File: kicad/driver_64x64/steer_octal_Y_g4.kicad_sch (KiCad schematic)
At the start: 66 parts

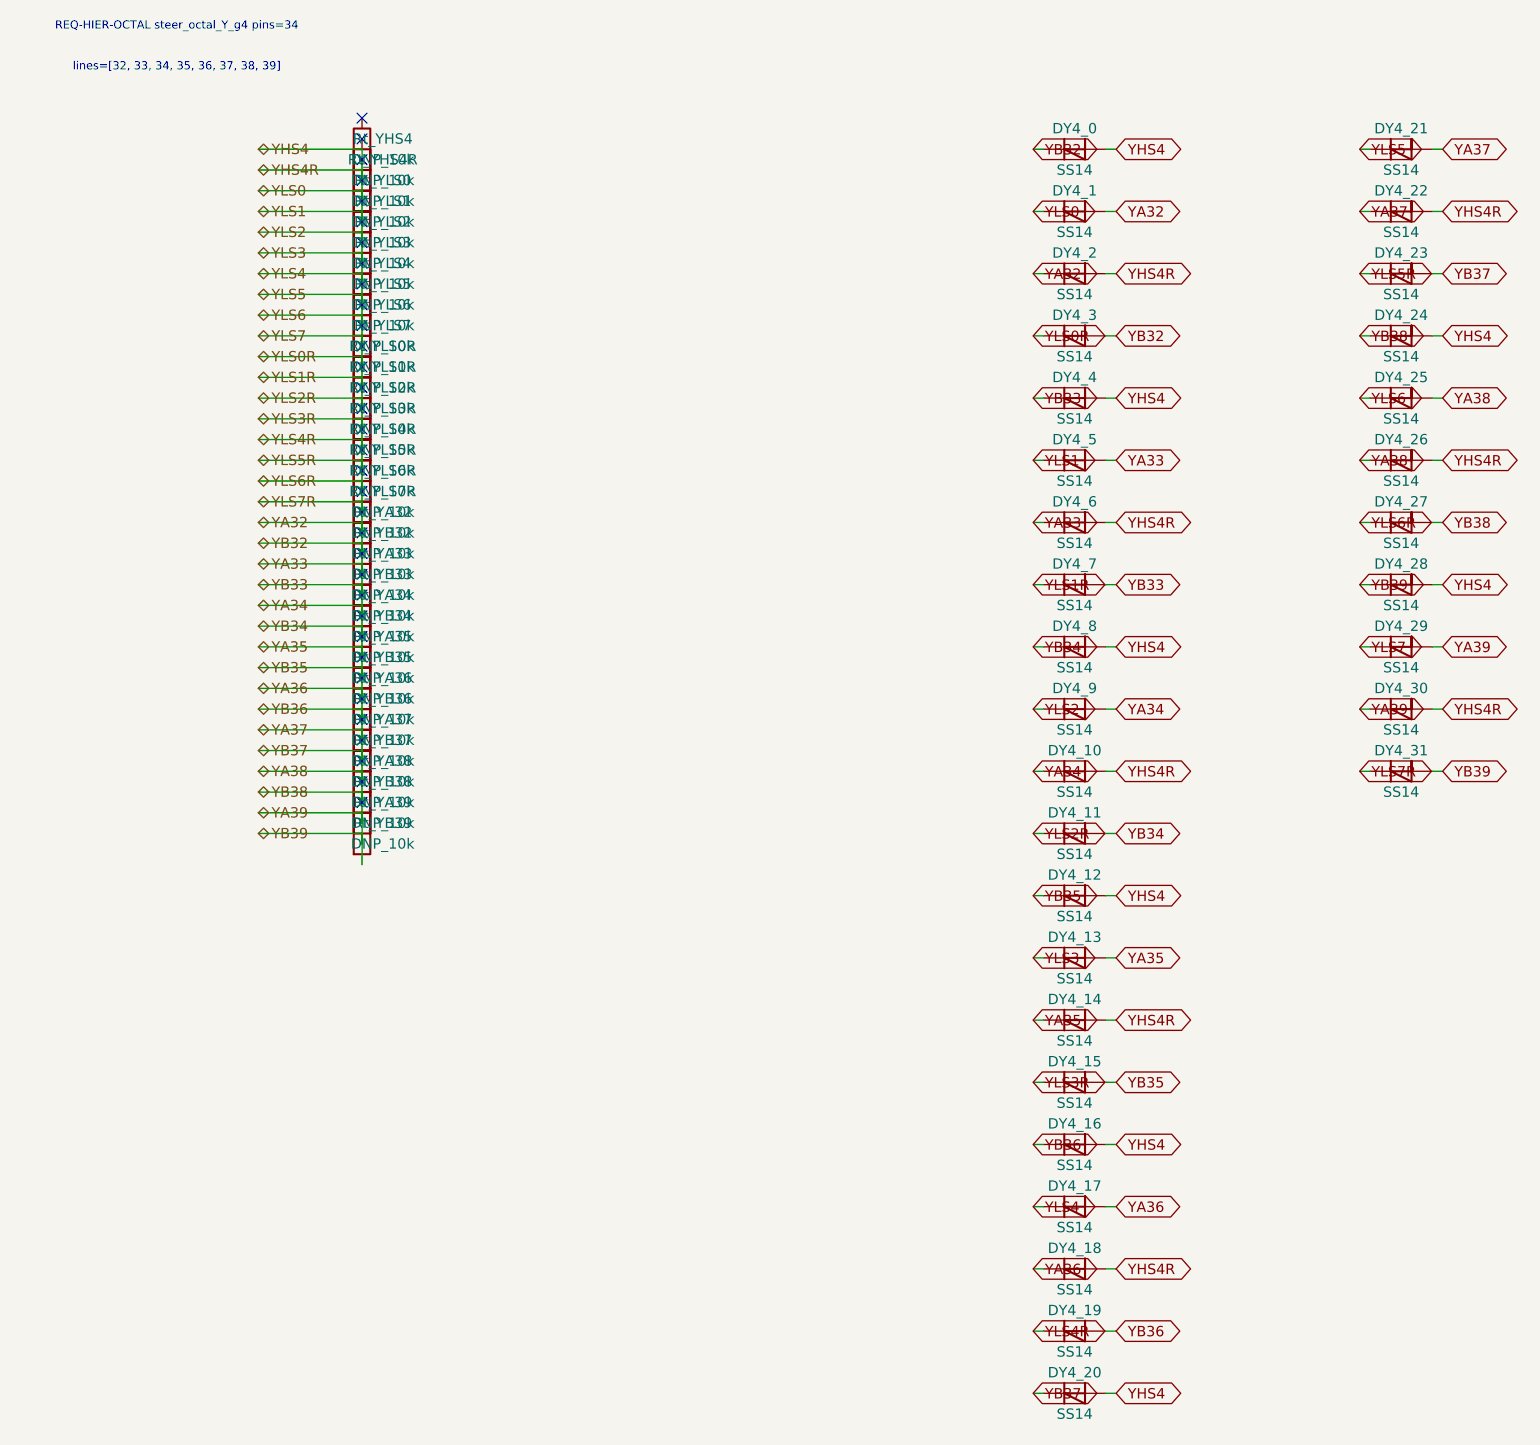
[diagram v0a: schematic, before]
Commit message: logical seperation into host and multiple decode/drive/steering boards
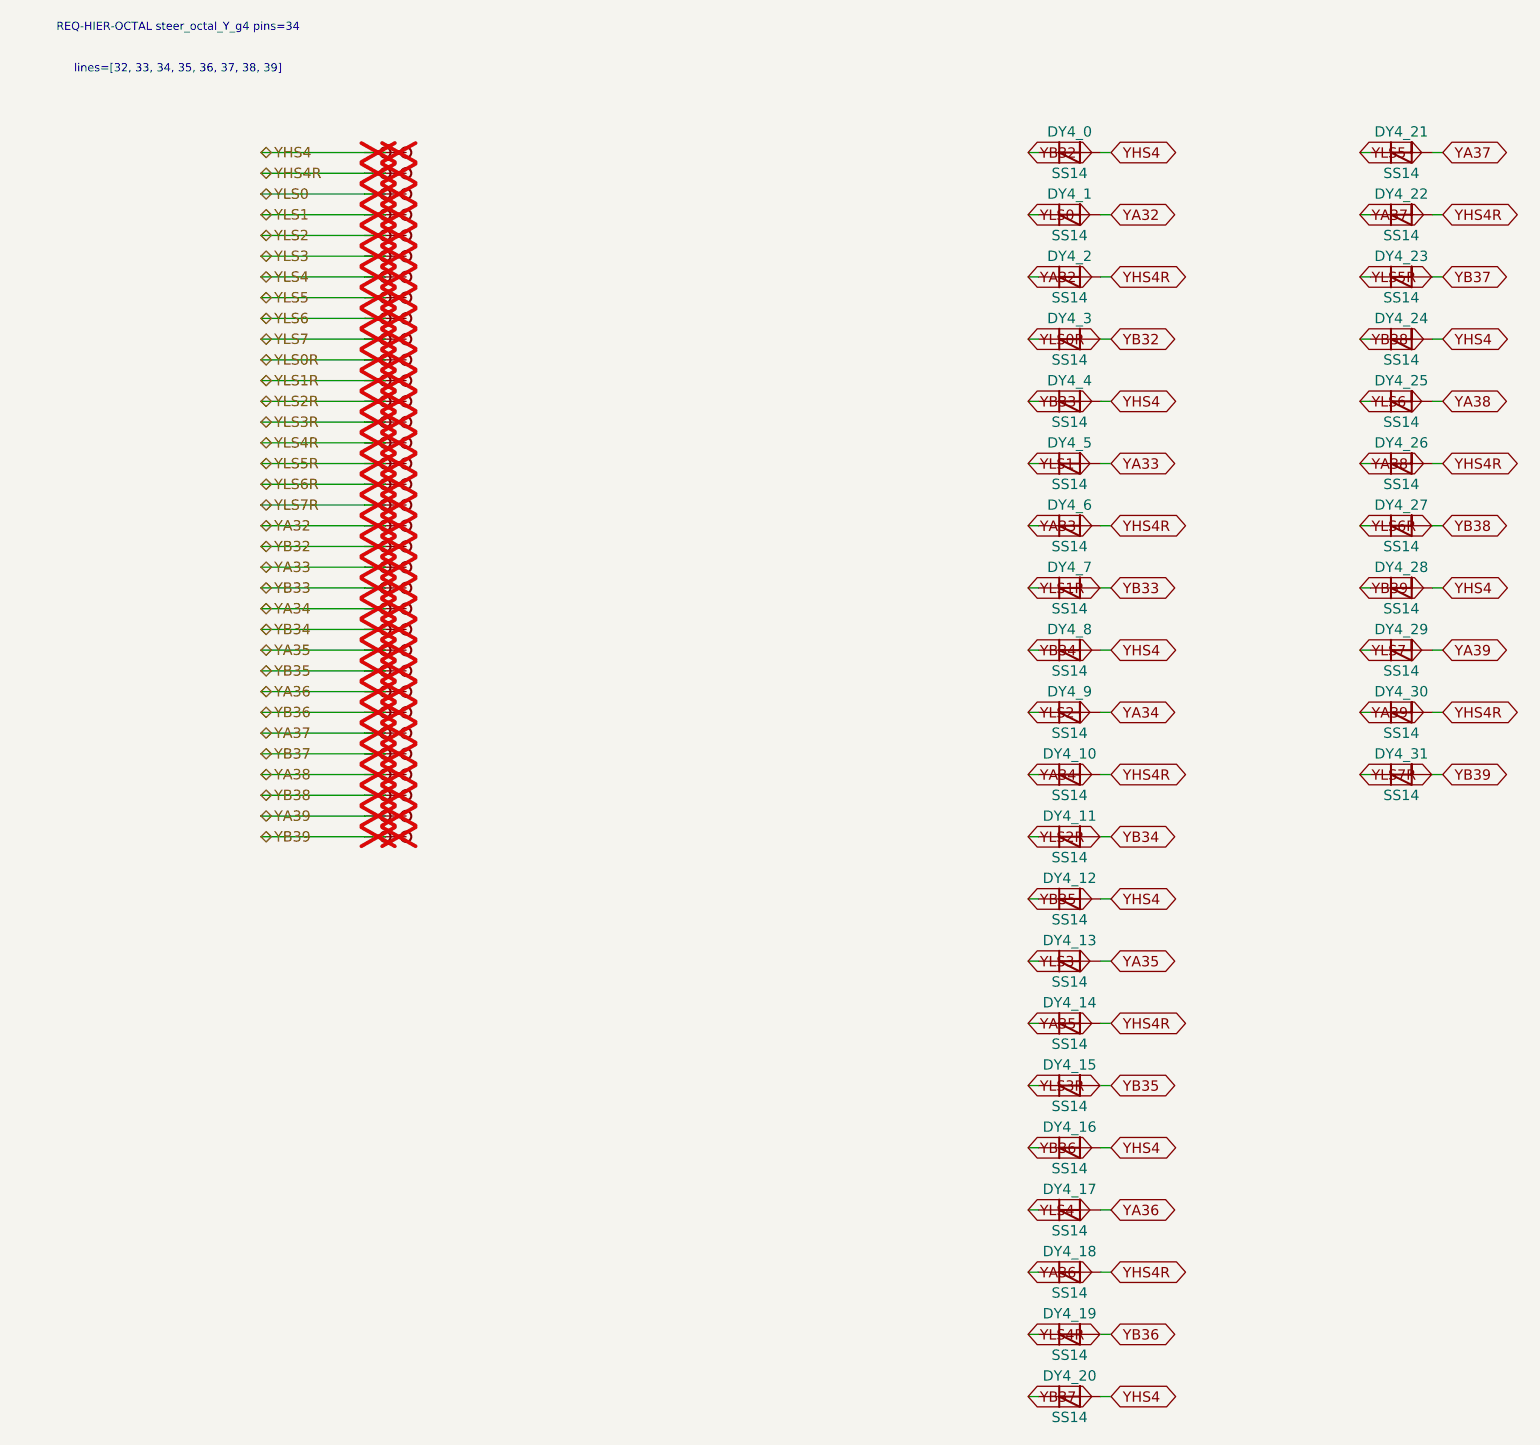
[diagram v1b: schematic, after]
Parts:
- removed Rt_YA32, Rt_YA33, Rt_YA34, Rt_YA35, Rt_YA36, Rt_YA37, Rt_YA38, Rt_YA39, Rt_YB32, Rt_YB33, Rt_YB34, Rt_YB35, Rt_YB36, Rt_YB37, Rt_YB38, Rt_YB39, Rt_YHS4, Rt_YHS4R, Rt_YLS0, Rt_YLS0R, Rt_YLS1, Rt_YLS1R, Rt_YLS2, Rt_YLS2R, Rt_YLS3, Rt_YLS3R, Rt_YLS4, Rt_YLS4R, Rt_YLS5, Rt_YLS5R, Rt_YLS6, Rt_YLS6R, Rt_YLS7, Rt_YLS7R: DNP_10k, symbol Device:R
- added TP_YA32, TP_YA32b, TP_YA33, TP_YA33b, TP_YA34, TP_YA34b, TP_YA35, TP_YA35b, TP_YA36, TP_YA36b, TP_YA37, TP_YA37b, TP_YA38, TP_YA38b, TP_YA39, TP_YA39b, TP_YB32, TP_YB32b, TP_YB33, TP_YB33b, TP_YB34, TP_YB34b, TP_YB35, TP_YB35b, TP_YB36, TP_YB36b, TP_YB37, TP_YB37b, TP_YB38, TP_YB38b, TP_YB39, TP_YB39b, TP_YHS4, TP_YHS4R, TP_YHS4Rb, TP_YHS4b, TP_YLS0, TP_YLS0R, TP_YLS0Rb, TP_YLS0b, TP_YLS1, TP_YLS1R, TP_YLS1Rb, TP_YLS1b, TP_YLS2, TP_YLS2R, TP_YLS2Rb, TP_YLS2b, TP_YLS3, TP_YLS3R, TP_YLS3Rb, TP_YLS3b, TP_YLS4, TP_YLS4R, TP_YLS4Rb, TP_YLS4b, TP_YLS5, TP_YLS5R, TP_YLS5Rb, TP_YLS5b, TP_YLS6, TP_YLS6R, TP_YLS6Rb, TP_YLS6b, TP_YLS7, TP_YLS7R, TP_YLS7Rb, TP_YLS7b: Stub, symbol CMR:Stub
- DY4_0, DY4_1, DY4_10, DY4_11, DY4_12, DY4_13, DY4_14, DY4_15, DY4_16, DY4_17, DY4_18, DY4_19, DY4_2, DY4_20, DY4_21, DY4_22, DY4_23, DY4_24, DY4_25, DY4_26, DY4_27, DY4_28, DY4_29, DY4_3, DY4_30, DY4_31, DY4_4, DY4_5, DY4_6, DY4_7, DY4_8, DY4_9: symbol Device:D_Schottky -> CMR:D_Schottky
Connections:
- net YA32: now also TP_YA32.1, TP_YA32b.1; no longer DY4_0.1 (K), DY4_0.2 (A), DY4_1.1 (K), DY4_10.1 (K), DY4_10.2 (A), DY4_11.1 (K), DY4_11.2 (A), DY4_12.1 (K), DY4_12.2 (A), DY4_13.1 (K), DY4_13.2 (A), DY4_14.1 (K), DY4_14.2 (A), DY4_15.1 (K), DY4_15.2 (A), DY4_16.1 (K), DY4_16.2 (A), DY4_17.1 (K), DY4_17.2 (A), DY4_18.1 (K), DY4_18.2 (A), DY4_19.1 (K), DY4_19.2 (A), DY4_2.2 (A), DY4_20.1 (K), DY4_20.2 (A), DY4_21.1 (K), DY4_21.2 (A), DY4_22.1 (K), DY4_22.2 (A), DY4_23.1 (K), DY4_23.2 (A), DY4_24.1 (K), DY4_24.2 (A), DY4_25.1 (K), DY4_25.2 (A), DY4_26.1 (K), DY4_26.2 (A), DY4_27.1 (K), DY4_27.2 (A), DY4_28.1 (K), DY4_28.2 (A), DY4_29.1 (K), DY4_29.2 (A), DY4_3.1 (K), DY4_3.2 (A), DY4_30.1 (K), DY4_30.2 (A), DY4_31.1 (K), DY4_31.2 (A), DY4_4.1 (K), DY4_4.2 (A), DY4_5.1 (K), DY4_5.2 (A), DY4_6.1 (K), DY4_6.2 (A), DY4_7.1 (K), DY4_7.2 (A), DY4_8.1 (K), DY4_8.2 (A), DY4_9.1 (K), DY4_9.2 (A)
- new net YA33: DY4_5.2 (A), DY4_6.1 (K), TP_YA33.1, TP_YA33b.1
- new net YA34: DY4_10.1 (K), DY4_9.2 (A), TP_YA34.1, TP_YA34b.1
- new net YA35: DY4_13.2 (A), DY4_14.1 (K), TP_YA35.1, TP_YA35b.1
- new net YA36: DY4_17.2 (A), DY4_18.1 (K), TP_YA36.1, TP_YA36b.1
- new net YA37: DY4_21.2 (A), DY4_22.1 (K), TP_YA37.1, TP_YA37b.1
- new net YA38: DY4_25.2 (A), DY4_26.1 (K), TP_YA38.1, TP_YA38b.1
- new net YA39: DY4_29.2 (A), DY4_30.1 (K), TP_YA39.1, TP_YA39b.1
- new net YB32: DY4_0.1 (K), DY4_3.2 (A), TP_YB32.1, TP_YB32b.1
- new net YB33: DY4_4.1 (K), DY4_7.2 (A), TP_YB33.1, TP_YB33b.1
- new net YB34: DY4_11.2 (A), DY4_8.1 (K), TP_YB34.1, TP_YB34b.1
- new net YB35: DY4_12.1 (K), DY4_15.2 (A), TP_YB35.1, TP_YB35b.1
- new net YB36: DY4_16.1 (K), DY4_19.2 (A), TP_YB36.1, TP_YB36b.1
- new net YB37: DY4_20.1 (K), DY4_23.2 (A), TP_YB37.1, TP_YB37b.1
- new net YB38: DY4_24.1 (K), DY4_27.2 (A), TP_YB38.1, TP_YB38b.1
- new net YB39: DY4_28.1 (K), DY4_31.2 (A), TP_YB39.1, TP_YB39b.1
- new net YHS4: DY4_0.2 (A), DY4_12.2 (A), DY4_16.2 (A), DY4_20.2 (A), DY4_24.2 (A), DY4_28.2 (A), DY4_4.2 (A), DY4_8.2 (A), TP_YHS4.1, TP_YHS4b.1
- new net YHS4R: DY4_10.2 (A), DY4_14.2 (A), DY4_18.2 (A), DY4_2.2 (A), DY4_22.2 (A), DY4_26.2 (A), DY4_30.2 (A), DY4_6.2 (A), TP_YHS4R.1, TP_YHS4Rb.1
- new net YLS0: DY4_1.1 (K), TP_YLS0.1, TP_YLS0b.1
- new net YLS0R: DY4_3.1 (K), TP_YLS0R.1, TP_YLS0Rb.1
- new net YLS1: DY4_5.1 (K), TP_YLS1.1, TP_YLS1b.1
- new net YLS1R: DY4_7.1 (K), TP_YLS1R.1, TP_YLS1Rb.1
- new net YLS2: DY4_9.1 (K), TP_YLS2.1, TP_YLS2b.1
- new net YLS2R: DY4_11.1 (K), TP_YLS2R.1, TP_YLS2Rb.1
- new net YLS3: DY4_13.1 (K), TP_YLS3.1, TP_YLS3b.1
- new net YLS3R: DY4_15.1 (K), TP_YLS3R.1, TP_YLS3Rb.1
- new net YLS4: DY4_17.1 (K), TP_YLS4.1, TP_YLS4b.1
- new net YLS4R: DY4_19.1 (K), TP_YLS4R.1, TP_YLS4Rb.1
- new net YLS5: DY4_21.1 (K), TP_YLS5.1, TP_YLS5b.1
- new net YLS5R: DY4_23.1 (K), TP_YLS5R.1, TP_YLS5Rb.1
- new net YLS6: DY4_25.1 (K), TP_YLS6.1, TP_YLS6b.1
- new net YLS6R: DY4_27.1 (K), TP_YLS6R.1, TP_YLS6Rb.1
- new net YLS7: DY4_29.1 (K), TP_YLS7.1, TP_YLS7b.1
- new net YLS7R: DY4_31.1 (K), TP_YLS7R.1, TP_YLS7Rb.1
- no-connect marks 34 -> 0
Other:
- moved on the sheet: DY4_0, DY4_1, DY4_10, DY4_11, DY4_12, DY4_13, DY4_14, DY4_15, DY4_16, DY4_17, DY4_18, DY4_19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
